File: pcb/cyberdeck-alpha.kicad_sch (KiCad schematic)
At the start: 516 parts, among them J1 CPU_FAN, J10 Conn_01x30, J11 Conn_01x22, J12 HDMI_C_1.3, J13 USB_C_Receptacle_USB2.0_16P, J14 Conn_01x06, J15 Conn_02x20_Odd_Even, J16 1-2199119-5, J17 2199119-3, J18 SIM_Card, J19 TSOP77438TR, J2 GP_LB, J20 Conn_01x22, J21 DX07S024JJ2R1300, J22 USB3_A, J3 GP_RB, J4 JOYSTICK, J5 Conn_01x06_Pin, J6 USB_C_Receptacle_USB2.0_16P, J7 Conn_01x05, J8 PJ-342B, J9 SPK, Q1 IRLML6244, Q2 CJ2101, Q3 SI4174DY-T1-GE3_N-Channel_FET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, Q4 BSS138, Q5 IRLML6244, Q6 SI4174DY-T1-GE3_N-Channel_FET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, Q7 SI4174DY-T1-GE3_N-Channel_FET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, Q8 SI4174DY-T1-GE3_N-Channel_FET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, U1 W25Q128JVS, U10 TPS62180YZFR, U11 TPS62180YZFR, U12 SY6280_OCP, U13 FAN5333ASX, U14 USBLC6-2SC6, U15 SY6280_OCP, U16 BQ76905RGRR, U17 ATtiny202-SS, U18 TPS25751SRSMR, U19 HD3SS3220IRNHT, U2 STM32F072CBT6, U20 TPD4EUSB30DQAR, U21 TPD4EUSB30DQAR, U22 AT24CS01-SSHM, U3 XC6206, U4 BQ25792RQMR, U5 RP2040, U6 USBLC6-2SC6, U7 CH334R, U8 PAM8406AB, U9 PCM2706CPJT, X1 X322512MSB4SI, X2 X322512MSB4SI, X3 X322512MSB4SI

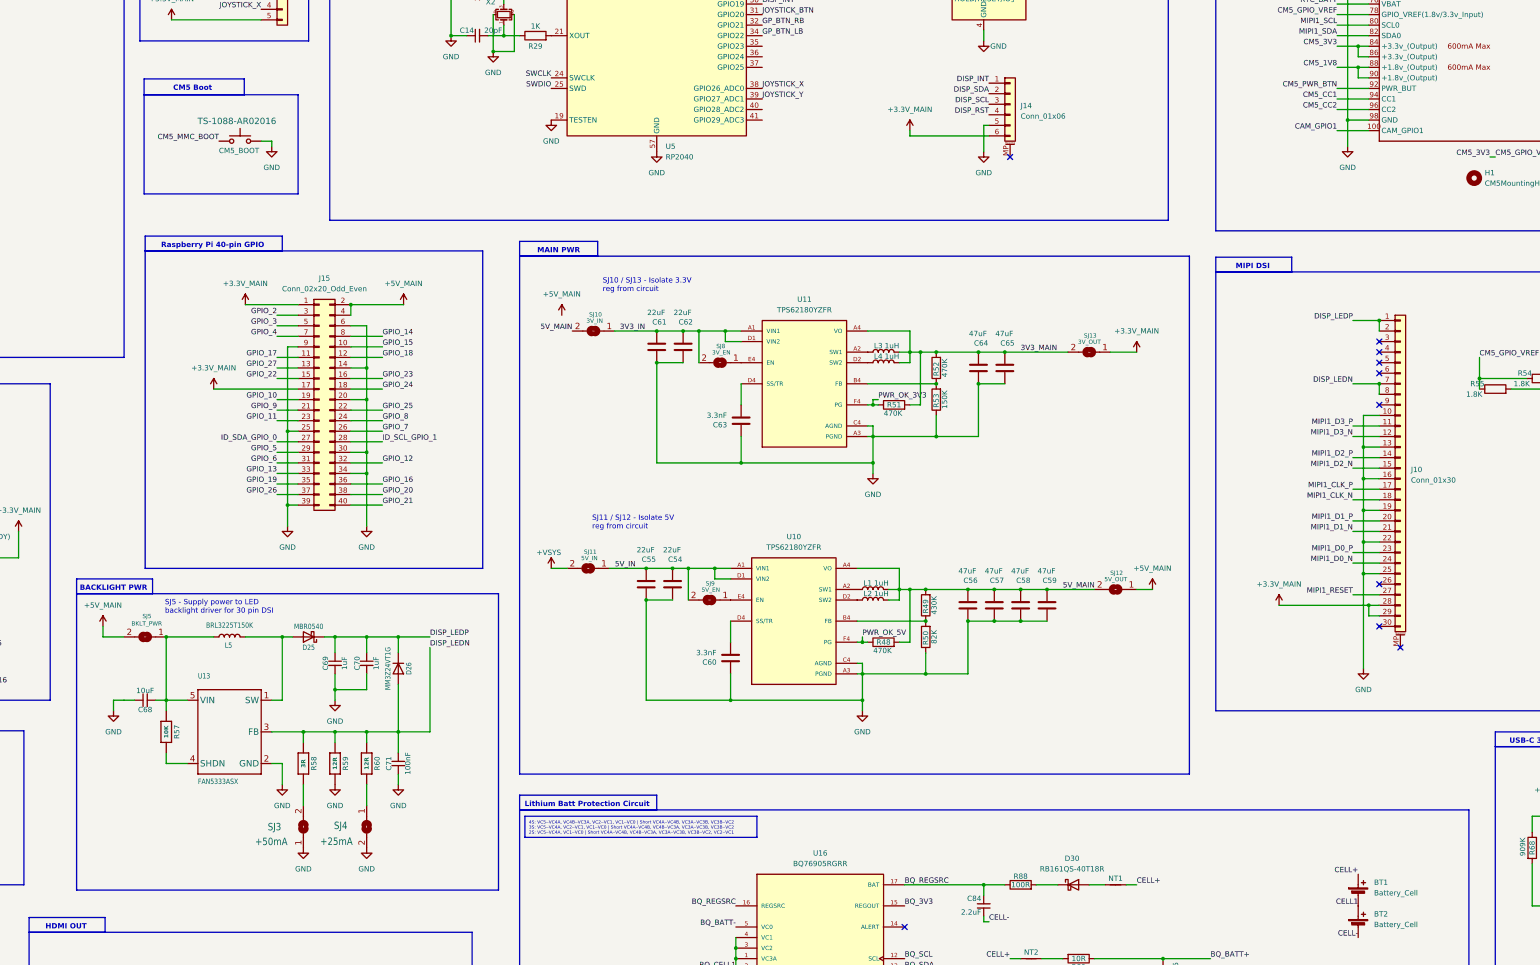
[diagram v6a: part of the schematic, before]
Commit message: removed 30p and length matched 22p
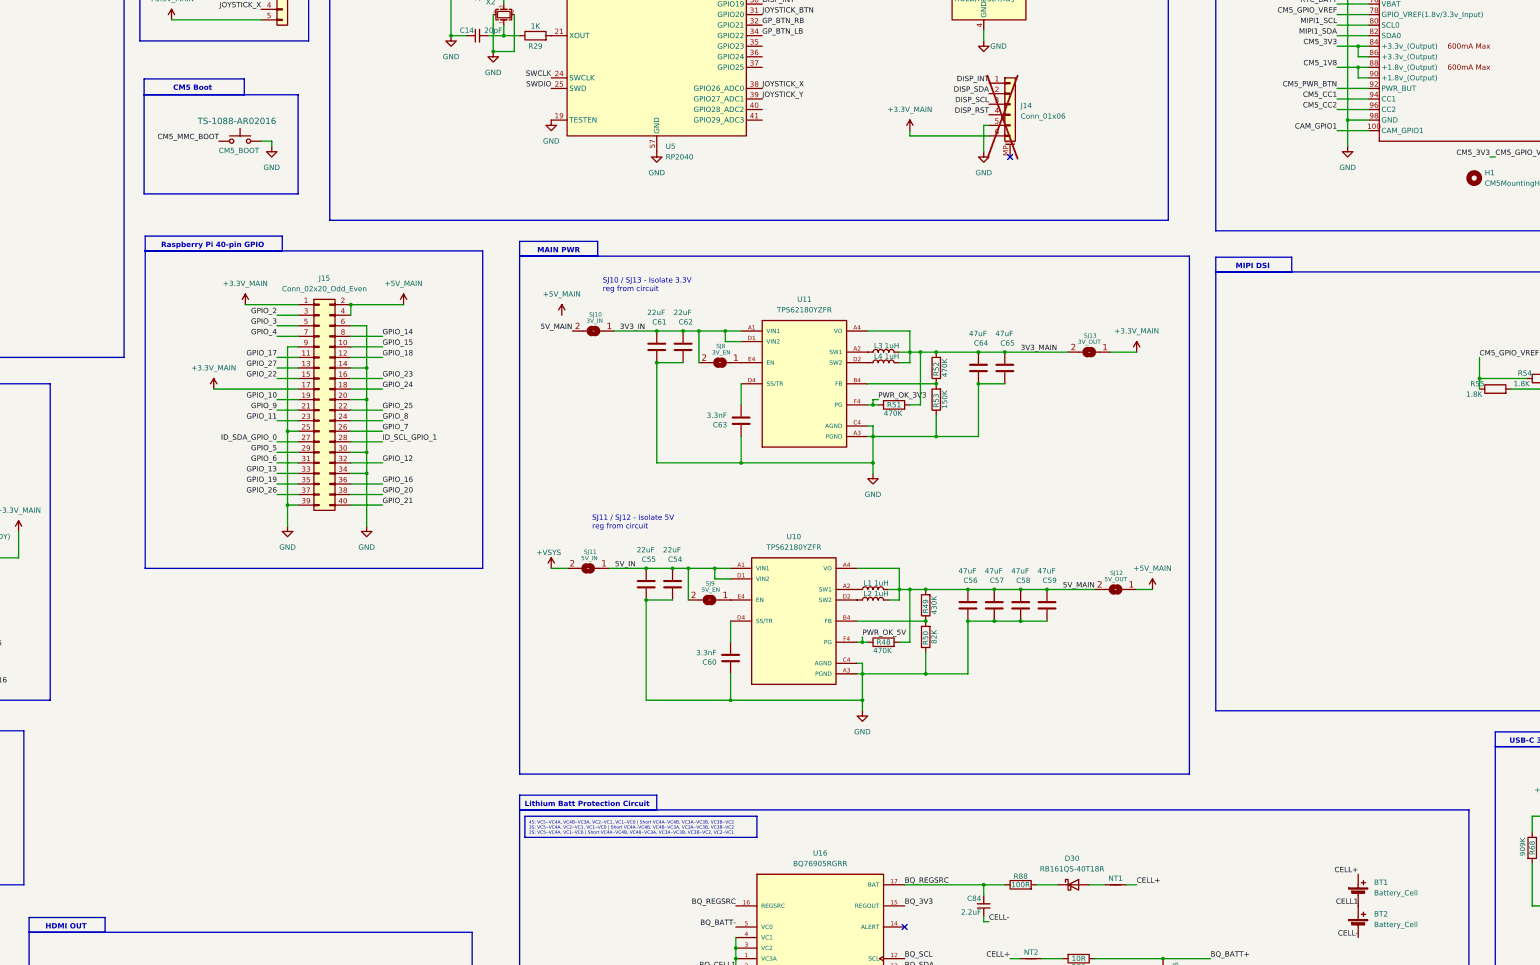
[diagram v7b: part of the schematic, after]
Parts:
- removed C68: 10uF, Capacitor_SMD:C_0805_2012Metric, symbol Device:C_Small
- removed C69, C70: 1uF, Capacitor_SMD:C_0805_2012Metric, symbol Device:C_Small
- removed C71: 100nF, Capacitor_SMD:C_0805_2012Metric, symbol Device:C_Small
- removed D25: MBR0540, Diode_SMD:D_SOD-123, symbol Diode:MBR0540
- removed D26: MM3Z24VT1G, Diode_SMD:D_SOD-323, symbol Device:D
- removed J10: Conn_01x30, LibraryGlobalFootprints:AFC07-S30ECA-00, symbol Connector_Generic_MountingPin:Conn_01x30_MountingPin
- removed L5: BRL3225T150K, Inductor_SMD:L_1210_3225Metric, symbol Device:L
- removed R57: 10K, Resistor_SMD:R_0805_2012Metric, symbol Adafruit TFP401 to 40pin TFT-eagle-import:RESISTOR0805_NOOUTLINE
- removed R58: 3R, Resistor_SMD:R_0805_2012Metric, symbol Adafruit TFP401 to 40pin TFT-eagle-import:RESISTOR0805_NOOUTLINE
- removed R59, R60: 12R, Resistor_SMD:R_0805_2012Metric, symbol Adafruit TFP401 to 40pin TFT-eagle-import:RESISTOR0805_NOOUTLINE
- removed SJ3: +50mA, LibraryGlobalFootprints:SOLDERJUMPER_ARROW_NOPASTE, symbol Adafruit TFP401 to 40pin TFT-eagle-import:SOLDERJUMPER
- removed SJ4: +25mA, LibraryGlobalFootprints:SOLDERJUMPER_ARROW_NOPASTE, symbol Adafruit TFP401 to 40pin TFT-eagle-import:SOLDERJUMPER
- removed SJ5: BKLT_PWR, LibraryGlobalFootprints:SOLDERJUMPER_ARROW_NOPASTE, symbol Adafruit TFP401 to 40pin TFT-eagle-import:SOLDERJUMPER
- removed U13: FAN5333ASX, Package_TO_SOT_SMD:SOT-23-5, symbol Adafruit TFP401 to 40pin TFT-eagle-import:VREG_FAN5331
- J14: now not fitted; now left out of the parts list
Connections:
- no-connect marks 114 -> 106
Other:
- note removed: "BACKLIGHT PWR"
